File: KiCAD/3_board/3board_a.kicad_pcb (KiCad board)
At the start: 2 copper layers, 95 x 99.5 mm, 73 parts, among them J1 USB_C_Receptacle_USB2.0_14P, J2 Conn_01x03_Socket, SW1 Memory Reset, SW17_W SW_Push, SW18_DOWN SW_Push, SW19_LEFT SW_Push, SW20_RIGHT SW_Push, SW8_DP SW_Push, U1 RP2040, U2 AMS1117-3.3_SOT223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

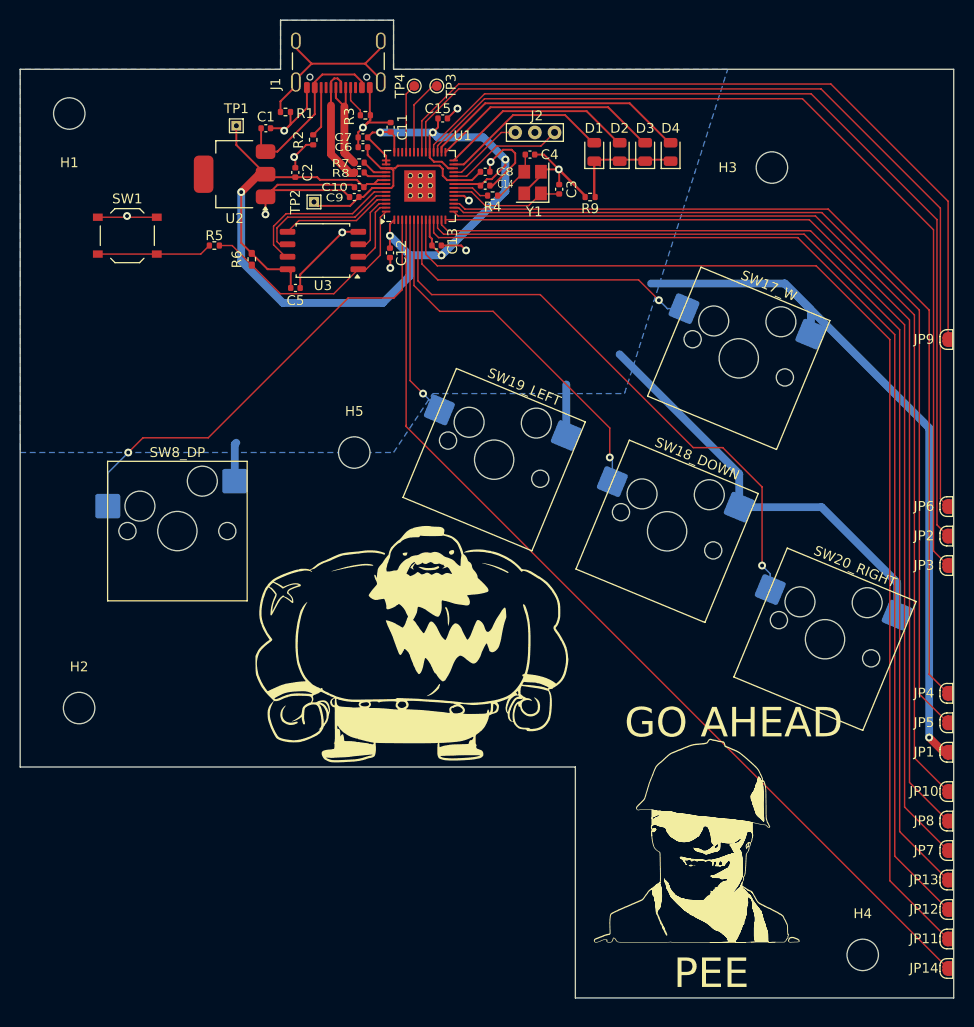
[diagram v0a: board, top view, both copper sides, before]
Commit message: Correct 27ohm resistor footprint to 0603 and add 10mm button
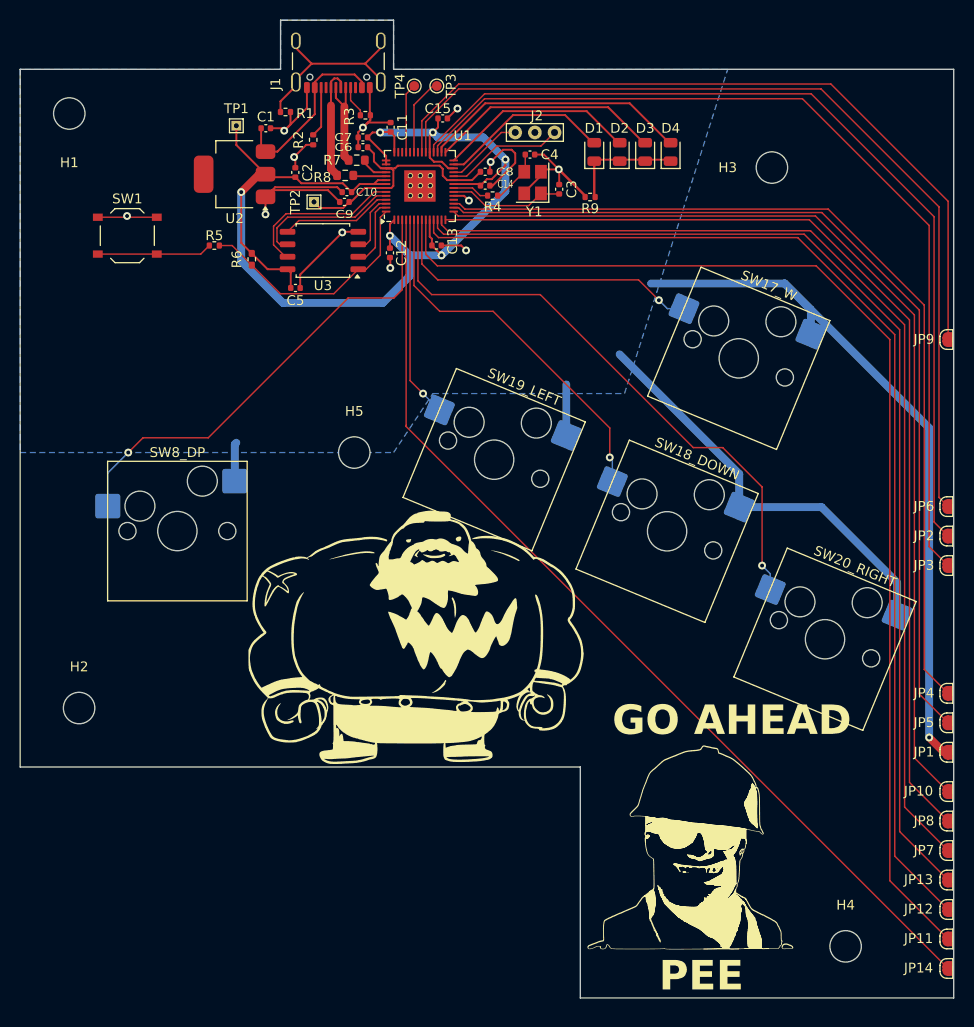
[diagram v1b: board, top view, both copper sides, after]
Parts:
- R7, R8: footprint Resistor_SMD:R_0402_1005Metric -> Resistor_SMD:R_0603_1608Metric
- moved H4 1.95 mm to (128.0, 114.2)
- moved R8 1.46 mm to (77.1, 35.8)
- moved C10 1.35 mm to (77.2, 37.5)
- moved C9 1.12 mm to (77.0, 38.5)
- moved R7 0.35 mm to (78.2, 34.2)
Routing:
- net GND: track 213.1 -> 211.0 mm
- net Net-(U1-USB_DP): track 2.39 -> 3.55 mm
- net Net-(D1-K): track 12.2 -> 11.4 mm
- net /Main/D+: track 12.5 -> 11.6 mm
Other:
- outline, holes or cut-outs redrawn
